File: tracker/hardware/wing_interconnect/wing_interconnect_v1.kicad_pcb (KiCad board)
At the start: 2 copper layers, 130 x 11 mm, 16 parts

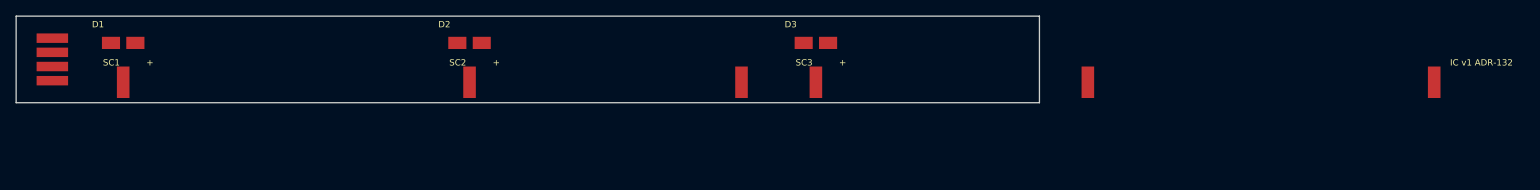
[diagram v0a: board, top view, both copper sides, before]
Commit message: feat(wing): 2-pin tab, GND+RF_FEED removed as dead copper, board is a small connector (ADR-134) (#286)
* feat(wing): foam wing geometry of record + ADR-130 (no PCB, parametric renders)

The wing stopped being a PCB when ADR-117 (Accepted by operator, 2026-10-15)
replaced the FR4 carrier with a bought XPS/Depron sheet. A foam wing has no
kicad_pcb, so `kicad-cli pcb render` has nothing to draw and the ONLY wing render
in the repo remained the RETIRED wing_board_v9 -- which is why the operator's
render still showed cells lying flat on copper.

Adds the missing geometry of record, parametric and cited:

* docs/analysis/foam_wing_geometry.py -- mass + VRML. Subtraction shown:
  cell 1.382 g (operator's own weighing) x 3 or 6; carrier = 0.1*rho*t*145.0 cm2;
  mount 0.15 g/cell (NIBBB measured, PANEL-MOUNTING-OFF-BOARD.md sec 2).
    EPS 3 mm SS 5.249 g | XPS 3 mm SS 5.988 g | XPS 6 mm SS 7.381 g
    EPS 3 mm DS 9.845 g | XPS 3 mm DS 10.584 g
    retired FR4 0.6 mm full-area 20.26 g (carrier 15.665 g)
* docs/analysis/render_foam_wing.py -- 6 PNG renders from the SAME parametric
  data (no VRML viewer on this host; matplotlib only), docs/fab/wing-3d/.
* docs/analysis/FOAM-WING-GEOMETRY-AND-MASS.md -- the two constructions (A foam
  plate, B foam spine), double-sided as option C, and the out-of-plane risk that
  picks the thickness; records that an earlier claim ("foam was never costed")
  was FALSE -- WING-MASS-FROM-MEASURED-CELLS.md sec 2 has the table and ADR-117
  accepted it.
* docs/analysis/WING-CUTOFF-AND-YAW.md -- cut survivability is ONE hub-side part
  (ADR-054 sec 2.2: without D_BP<n> the first cut kills the array, 0.00 W; with it
  only that wing's cells are lost). There is NO yaw authority (wing-jettison.md:
  "rotates slowly with no attitude control"), so shedding a wing neither helps nor
  hurts turn-around.
* docs/adr/130-foam-wing-geometry-authority.md -- number verified free via
  scripts/adr_next_number.py (--number 130 and --path both exit 0) and across 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
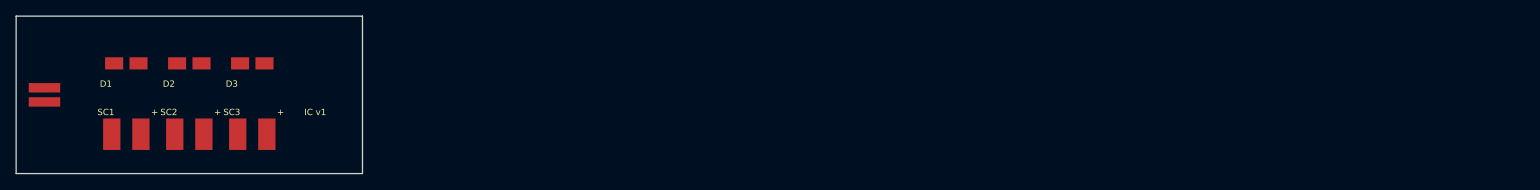
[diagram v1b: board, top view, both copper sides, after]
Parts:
- removed the ? at (4.60, 2.80)
- removed the ? at (180.2, 8.40)
- removed the ? at (12.1, 3.40)
- removed the ? at (15.2, 3.40)
- removed the ? at (56.0, 3.40)
- removed the ? at (59.1, 3.40)
- removed the ? at (100.0, 3.40)
- removed the ? at (103.2, 3.40)
- removed the ? at (4.60, 4.60)
- removed the ? at (4.60, 6.40)
- removed the ? at (4.60, 8.20)
- removed the ? at (13.6, 8.40)
- removed the ? at (92.2, 8.40)
- removed the ? at (57.6, 8.40)
- removed the ? at (136.2, 8.40)
- removed the ? at (101.6, 8.40)
- added ?: , wing_ic:J1, F.Cu at (3.60, 9.10)
- added ?: , wing_ic:D1, F.Cu at (15.6, 6.00)
- added ?: , wing_ic:D2, F.Cu at (20.4, 6.00)
- added ?: , wing_ic:D2, F.Cu at (23.6, 6.00)
- added ?: , wing_ic:D3, F.Cu at (28.4, 6.00)
- added ?: , wing_ic:D3, F.Cu at (31.6, 6.00)
- added ?: , wing_ic:J1, F.Cu at (3.60, 10.9)
- added ?: , wing_ic:SC1, F.Cu at (12.2, 15.0)
- added ?: , wing_ic:SC1, F.Cu at (15.8, 15.0)
- added ?: , wing_ic:SC2, F.Cu at (20.1, 15.0)
- added ?: , wing_ic:SC2, F.Cu at (23.9, 15.0)
- added ?: , wing_ic:SC3, F.Cu at (28.1, 15.0)
- added ?: , wing_ic:SC3, F.Cu at (31.9, 15.0)
- added ?: , wing_ic:D1, F.Cu at (12.4, 6.00)
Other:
- board size 130 x 11 mm -> 44 x 20 mm
- board text added: "IC v1"
- board text removed: "IC v1 ADR-132"
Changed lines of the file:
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@@
   (net 3 "SOLAR_MID2")
   (net 4 "SOLAR_N")
-  (net 5 "GND")
-  (net 6 "RF_FEED")
-  (gr_line (start 0 0) (end 130 0) (stroke (width 0.1) (type solid)) (layer "Edge.Cuts"))
-  (gr_line (start 130 0) (end 130 11) (stroke (width 0.1) (type solid)) (layer "Edge.Cuts"))
-  (gr_line (start 130 11) (end 0 11) (stroke (width 0.1) (type solid)) (layer "Edge.Cuts"))
-  (gr_line (start 0 11) (end 0 0) (stroke (width 0.1) (type solid)) (layer "Edge.Cuts"))
-  (footprint "wing_ic:J1" (layer "F.Cu") (at 4.6 2.8)
+  (gr_line (start 0 0) (end 44 0) (stroke (width 0.1) (type solid)) (layer "Edge.Cuts"))
+  (gr_line (start 44 0) (end 44 20) (stroke (width 0.1) (type solid)) (layer "Edge.Cuts"))
+  (gr_line (start 44 20) (end 0 20) (stroke (width 0.1) (type solid)) (layer "Edge.Cuts"))
+  (gr_line (start 0 20) (end 0 0) (stroke (width 0.1) (type solid)) (layer "Edge.Cuts"))
+  (footprint "wing_ic:J1" (layer "F.Cu") (at 3.6 9.1)
     (pad "1" smd rect (at 0 0) (size 4 1.2) (layers "F.Cu" "F.Paste" "F.Mask") (net 1 "SOLAR_P"))
   )
-  (footprint "wing_ic:J1" (layer "F.Cu") (at 4.6 4.6)
-    (pad "2" smd rect (at 0 0) (size 4 1.2) (layers "F.Cu" "F.Paste" "F.Mask") (net 2 "SOLAR_MID1"))
+  (footprint "wing_ic:J1" (layer "F.Cu") (at 3.6 10.9)
+    (pad "2" smd rect (at 0 0) (size 4 1.2) (layers "F.Cu" "F.Paste" "F.Mask") (net 4 "SOLAR_N"))
   )
-  (footprint "wing_ic:J1" (layer "F.Cu") (at 4.6 6.4)
-    (pad "3" smd rect (at 0 0) (size 4 1.2) (layers "F.Cu" "F.Paste" "F.Mask") (net 3 "SOLAR_MID2"))
+  (footprint "wing_ic:SC1" (layer "F.Cu") (at 12.15 15)
+    (pad "1" smd rect (at 0 0) (size 2.2 4) (layers "F.Cu" "F.Paste" "F.Mask") (net 1 "SOLAR_P"))
   )
-  (footprint "wing_ic:J1" (layer "F.Cu") (at 4.6 8.2)
-    (pad "4" smd rect (at 0 0) (size 4 1.2) (layers "F.Cu" "F.Paste" "F.Mask") (net 4 "SOLAR_N"))
+  (footprint "wing_ic:SC1" (layer "F.Cu") (at 15.85 15)
+    (pad "2" smd rect (at 0 0) (size 2.2 4) (layers "F.Cu" "F.Paste" "F.Mask") (net 2 "SOLAR_MID1"))
   )
-  (footprint "wing_ic:SC1" (layer "F.Cu") (at 13.6 8.4)
-    (pad "1" smd rect (at 0 0) (size 1.6 4) (layers "F.Cu" "F.Paste" "F.Mask") (net 1 "SOLAR_P"))
+  (footprint "wing_ic:SC2" (layer "F.Cu") (at 20.15 15)
+    (pad "1" smd rect (at 0 0) (size 2.2 4) (layers "F.Cu" "F.Paste" "F.Mask") (net 2 "SOLAR_MID1"))
   )
-  (footprint "wing_ic:SC1" (layer "F.Cu") (at 92.15 8.4)
-    (pad "2" smd rect (at 0 0) (size 1.6 4) (layers "F.Cu" "F.Paste" "F.Mask") (net 2 "SOLAR_MID1"))
+  (footprint "wing_ic:SC2" (layer "F.Cu") (at 23.85 15)
+    (pad "2" smd rect (at 0 0) (size 2.2 4) (layers "F.Cu" "F.Paste" "F.Mask") (net 3 "SOLAR_MID2"))
   )
-  (footprint "wing_ic:SC2" (layer "F.Cu") (at 57.6 8.4)
-    (pad "1" smd rect (at 0 0) (size 1.6 4) (layers "F.Cu" "F.Paste" "F.Mask") (net 2 "SOLAR_MID1"))
+  (footprint "wing_ic:SC3" (layer "F.Cu") (at 28.15 15)
+    (pad "1" smd rect (at 0 0) (size 2.2 4) (layers "F.Cu" "F.Paste" "F.Mask") (net 3 "SOLAR_MID2"))
   )
-  (footprint "wing_ic:SC2" (layer "F.Cu") (at 136.15 8.4)
-    (pad "2" smd rect (at 0 0) (size 1.6 4) (layers "F.Cu" "F.Paste" "F.Mask") (net 3 "SOLAR_MID2"))
+  (footprint "wing_ic:SC3" (layer "F.Cu") (at 31.85 15)
+    (pad "2" smd rect (at 0 0) (size 2.2 4) (layers "F.Cu" "F.Paste" "F.Mask") (net 4 "SOLAR_N"))
   )
-  (footprint "wing_ic:SC3" (layer "F.Cu") (at 101.6 8.4)
-    (pad "1" smd rect (at 0 0) (size 1.6 4) (layers "F.Cu" "F.Paste" "F.Mask") (net 3 "SOLAR_MID2"))
-  )
-  (footprint "wing_ic:SC3" (layer "F.Cu") (at 180.15 8.4)
-    (pad "2" smd rect (at 0 0) (size 1.6 4) (layers "F.Cu" "F.Paste" "F.Mask") (net 4 "SOLAR_N"))
-  )
-  (footprint "wing_ic:D1" (layer "F.Cu") (at 12.05 3.4)
+  (footprint "wing_ic:D1" (layer "F.Cu") (at 12.45 6)
     (pad "1" smd rect (at 0 0) (size 2.3 1.55) (layers "F.Cu" "F.Paste" "F.Mask") (net 1 "SOLAR_P"))
   )
-  (footprint "wing_ic:D1" (layer "F.Cu") (at 15.15 3.4)
+  (footprint "wing_ic:D1" (layer "F.Cu") (at 15.55 6)
     (pad "2" smd rect (at 0 0) (size 2.3 1.55) (layers "F.Cu" "F.Paste" "F.Mask") (net 2 "SOLAR_MID1"))
   )
-  (footprint "wing_ic:D2" (layer "F.Cu") (at 56.05 3.4)
+  (footprint "wing_ic:D2" (layer "F.Cu") (at 20.45 6)
     (pad "1" smd rect (at 0 0) (size 2.3 1.55) (layers "F.Cu" "F.Paste" "F.Mask") (net 2 "SOLAR_MID1"))
   )
-  (footprint "wing_ic:D2" (layer "F.Cu") (at 59.15 3.4)
+  (footprint "wing_ic:D2" (layer "F.Cu") (at 23.55 6)
     (pad "2" smd rect (at 0 0) (size 2.3 1.55) (layers "F.Cu" "F.Paste" "F.Mask") (net 3 "SOLAR_MID2"))
   )
-  (footprint "wing_ic:D3" (layer "F.Cu") (at 100.05 3.4)
+  (footprint "wing_ic:D3" (layer "F.Cu") (at 28.45 6)
     (pad "1" smd rect (at 0 0) (size 2.3 1.55) (layers "F.Cu" "F.Paste" "F.Mask") (net 3 "SOLAR_MID2"))
   )
-  (footprint "wing_ic:D3" (layer "F.Cu") (at 103.15 3.4)
+  (footprint "wing_ic:D3" (layer "F.Cu") (at 31.55 6)
     (pad "2" smd rect (at 0 0) (size 2.3 1.55) (layers "F.Cu" "F.Paste" "F.Mask") (net 4 "SOLAR_N"))
   )
-  (gr_text "SC1" (at 12.1 5.9) (layer "F.SilkS") (effects (font (size 0.8 0.8) (thickness 0.15))))
-  (gr_text "+" (at 17 5.9) (layer "F.SilkS") (effects (font (size 0.8 0.8) (thickness 0.15))))
-  (gr_text "SC2" (at 56.1 5.9) (layer "F.SilkS") (effects (font (size 0.8 0.8) (thickness 0.15))))
-  (gr_text "+" (at 61 5.9) (layer "F.SilkS") (effects (font (size 0.8 0.8) (thickness 0.15))))
-  (gr_text "SC3" (at 100.1 5.9) (layer "F.SilkS") (effects (font (size 0.8 0.8) (thickness 0.15))))
-  (gr_text "+" (at 105 5.9) (layer "F.SilkS") (effects (font (size 0.8 0.8) (thickness 0.15))))
-  (gr_text "D1" (at 10.4 1.05) (layer "F.SilkS") (effects (font (size 0.8 0.8) (thickness 0.15))))
-  (gr_text "D2" (at 54.4 1.05) (layer "F.SilkS") (effects (font (size 0.8 0.8) (thickness 0.15))))
-  (gr_text "D3" (at 98.4 1.05) (layer "F.SilkS") (effects (font (size 0.8 0.8) (thickness 0.15))))
-  (gr_text "IC v1 ADR-132" (at 186.15 5.9) (layer "F.SilkS") (effects (font (size 0.8 0.8) (thickness 0.15))))
+  (gr_text "SC1" (at 11.4 12.2) (layer "F.SilkS") (effects (font (size 0.8 0.8) (thickness 0.15))))
+  (gr_text "+" (at 17.6 12.2) (layer "F.SilkS") (effects (font (size 0.8 0.8) (thickness 0.15))))
+  (gr_text "SC2" (at 19.4 12.2) (layer "F.SilkS") (effects (font (size 0.8 0.8) (thickness 0.15))))
+  (gr_text "+" (at 25.6 12.2) (layer "F.SilkS") (effects (font (size 0.8 0.8) (thickness 0.15))))
+  (gr_text "SC3" (at 27.4 12.2) (layer "F.SilkS") (effects (font (size 0.8 0.8) (thickness 0.15))))
+  (gr_text "+" (at 33.6 12.2) (layer "F.SilkS") (effects (font (size 0.8 0.8) (thickness 0.15))))
+  (gr_text "D1" (at 11.4 8.6) (layer "F.SilkS") (effects (font (size 0.8 0.8) (thickness 0.15))))
+  (gr_text "D2" (at 19.4 8.6) (layer "F.SilkS") (effects (font (size 0.8 0.8) (thickness 0.15))))
+  (gr_text "D3" (at 27.4 8.6) (layer "F.SilkS") (effects (font (size 0.8 0.8) (thickness 0.15))))
+  (gr_text "IC v1" (at 38 12.2) (layer "F.SilkS") (effects (font (size 0.8 0.8) (thickness 0.15))))
 )

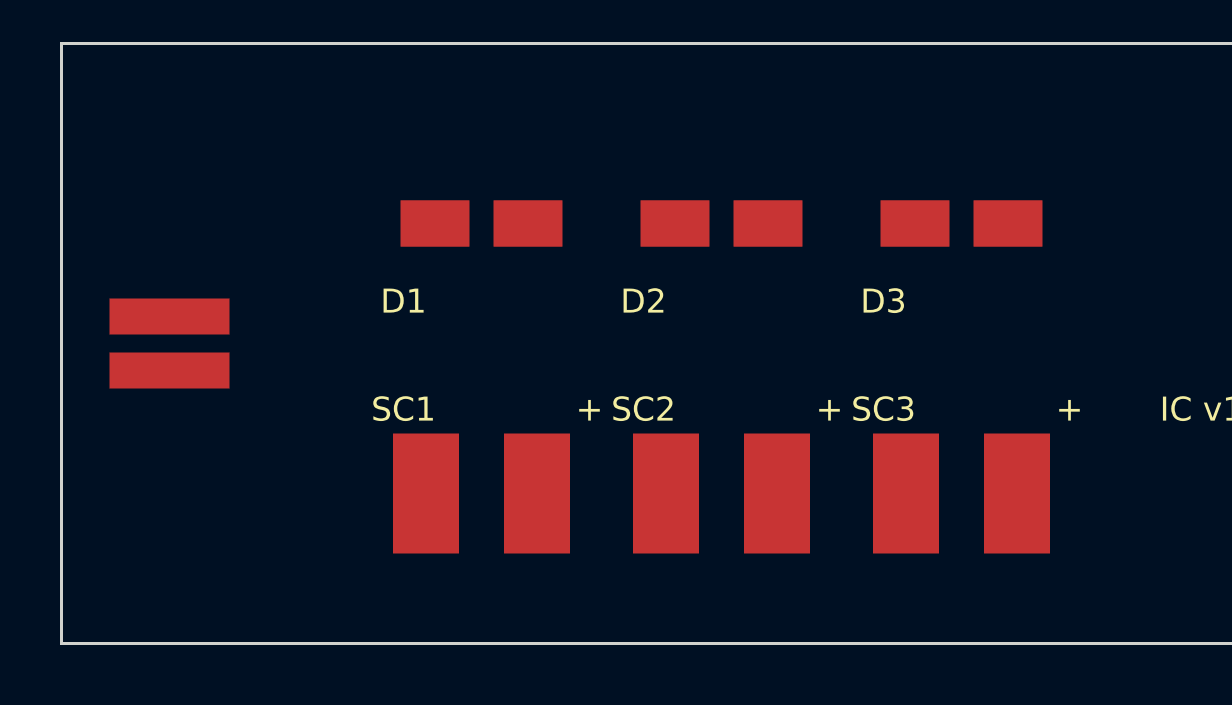
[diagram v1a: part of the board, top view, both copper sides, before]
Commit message: feat(wing): interconnect board ROUTED -- 0 unrouted, 0 electrical DRC violations
The wing interconnect board is now fully routed. DRC on the committed board:
  7 lib_footprint_issues   (generated footprints, no registered library -- same as hub)
  0 everything else        (no short, clearance, crossing, mask bridge, silk or edge)
KiCad's own connectivity engine, independent of DRC: unrouted = 0.
7 footprints, 14 pads, 34 tracks.

ROUTING IS TWO MECHANISMS, DELIBERATELY
  * deterministic geometry in the generator for the two COLLINEAR nets. SOLAR_P and
    SOLAR_N have pads at identical x, one row at y=6 and one at y=15, so they are straight
    vertical drops. P stays on F.Cu (its column at x=12.15 is left of every MID pad).
    N's horizontal escape runs on B.Cu -- on F.Cu it CANNOT work, because the pad rows sit
    at y=6 and y=15 and P's column spans exactly that range, so no clear y exists on one
    layer. Two vias lift it over.
  * the A* router for the two multi-pad nets:
    route_v10_astar.py --append --nets SOLAR_MID1,SOLAR_MID2  -> routed 2, failed 0.
  Router alone measured 2 of 4 nets maximum in every ordering tried (--promote included);
  making two nets trivial by construction is what closed the rest.

SIX DEFECTS FOUND AND FIXED, ALL MEASURED (docs/fab/wing-3d/ROUTING-STATUS.md sec 3)
  1 one footprint PER PAD -> 14 footprints for 7 parts (group pads by ref)
  2 removing fp_text reference to fix silk_overlap DESTROYED NET IDENTITY -- every ref read
    identical, so the router deduped SOLAR_P's 3 pads to 1 and silently skipped the net
    ("failed 0", 2 of 4 routed). Restored on F.Fab so silk stays clean and identity holds.
    LESSON: a silk fix must never touch the reference property.
  3 router clobber guard hardcoded "nfps < 20" / "expected 28" (the hub's count), so a
    7-part board could never be saved; now --expect-footprints, default 20, hub unchanged
  4 cells cx+-1.85 vs diodes cx+-1.55 staggered every net into a TRIANGLE; one PAD_DX make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
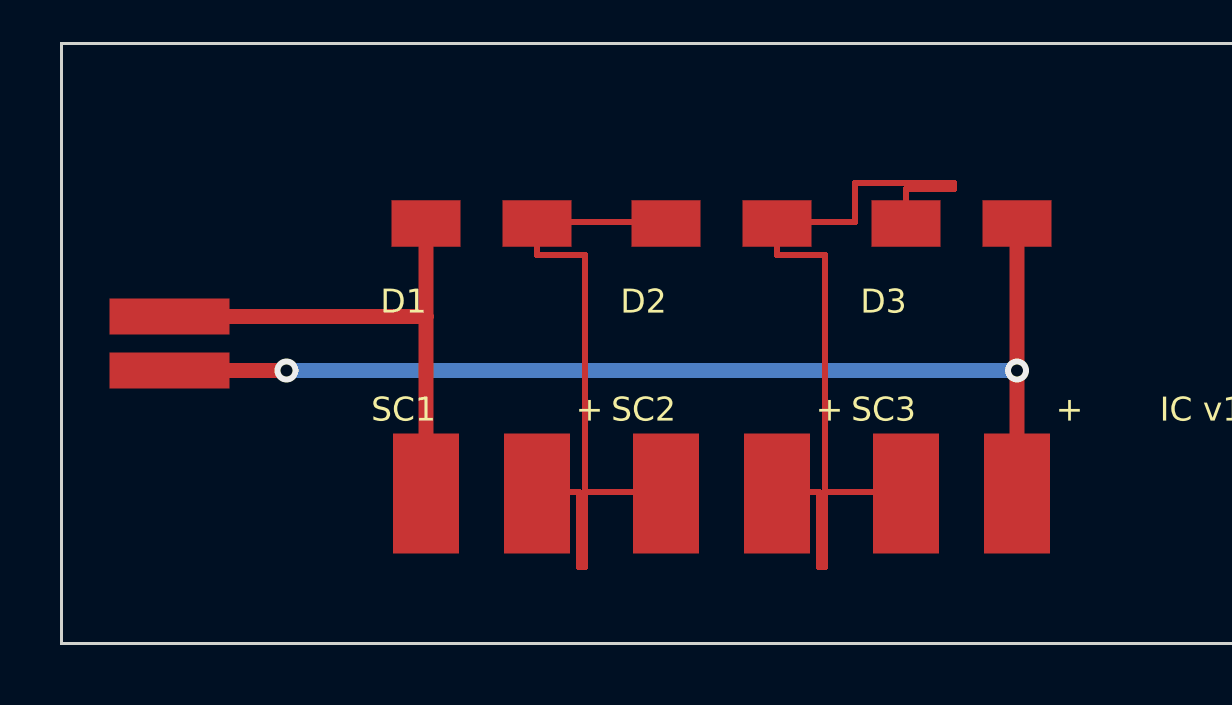
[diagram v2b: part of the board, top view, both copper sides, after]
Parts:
- removed ? (x2): , wing_ic:J1
- removed ? (x2): , wing_ic:D1
- removed ? (x2): , wing_ic:D2
- removed ? (x2): , wing_ic:D3
- removed ? (x2): , wing_ic:SC1
- removed ? (x2): , wing_ic:SC2
- removed ? (x2): , wing_ic:SC3
- added D1: , wing_ic:D1, F.Cu at (12.2, 6.00)
- added D2: , wing_ic:D2, F.Cu at (20.1, 6.00)
- added D3: , wing_ic:D3, F.Cu at (28.1, 6.00)
- added J1: , wing_ic:J1, F.Cu at (3.60, 9.10)
- added SC1: , wing_ic:SC1, F.Cu at (12.2, 15.0)
- added SC2: , wing_ic:SC2, F.Cu at (20.1, 15.0)
- added SC3: , wing_ic:SC3, F.Cu at (28.1, 15.0)
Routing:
- net SOLAR_N: track 0.00 -> 37.2 mm, vias 0 -> 2
- net SOLAR_MID2: track 0.00 -> 32.7 mm
- net SOLAR_MID1: track 0.00 -> 26.9 mm
- net SOLAR_P: track 0.00 -> 17.6 mm

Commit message: feat(wing): real wing_ic footprint library -- board is now DRC-clean, 0 violations (#292)
THE LAST FAB BLOCKER IS GONE. kicad-cli pcb drc --exit-code-violations now reports:

    Found 0 violations
    Found 0 unconnected items

Previously it reported 7 x lib_footprint_issues. Zero violations of ANY class -- no lib
warnings, no shorts, no clearance, no crossings, no mask bridges, no silk, no edge.

ROOT CAUSE WAS NAMING, NOT GEOMETRY
DRC said, seven times: "The current configuration does not include the footprint library
'wing_ic'." The board's pads were in the right places; they named a library that did not
exist, so nothing could resolve and the board could never be ordered.

THE FIX, following the pattern the repo already uses (balloon_flight.pretty + ${KIPRJMOD}):
  * tracker/hardware/wing_interconnect/wing_ic.pretty/ -- D_SMA_Wing, SolarTail_2P, Tab_2P
  * tracker/hardware/wing_interconnect/fp-lib-table -- registers it
  * tracker/hardware/build_wing_footprints.py -- deterministic generator (--check)

LAND GEOMETRY IS CARRIED OVER UNCHANGED, DELIBERATELY
The pads reproduce the board's existing patterns, NOT the stock vendor ones:
    stock Diode_SMD:D_SMA   2.5 x 1.8 at +-2.0
    this board              2.3 x 1.55 at +-1.85
Adopting the stock pattern would move every pad edge by up to 0.2 mm and invalidate the
routed copper from PR #289 -- to fix a NAMING problem. The house pattern is frozen as a
named library footprint and the deviation from the vendor land pattern is recorded rather
than silently adopted.

THE BOARD EMITS THE LIBRARY FOOTPRINT VERBATIM
Writing the body by hand produced 7 x lib_footprint_mismatch (measured): DRC compares the
board's embedded copy against the library file and any difference -- courtyard, pad order --
is a warning. build_wing_interconnect.py now reads the .kicad_mod and substitutes only the
origin, the reference and the per-pad nets, so a mismatch is impossible by construction.

FOUR DEFECTS FOUND WHILE DOING IT, ALL MEASURED
  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
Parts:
- D1: value (none) -> D_SMA_Wing; footprint wing_ic:D1 -> wing_ic:D_SMA_Wing
- D2: value (none) -> D_SMA_Wing; footprint wing_ic:D2 -> wing_ic:D_SMA_Wing
- D3: value (none) -> D_SMA_Wing; footprint wing_ic:D3 -> wing_ic:D_SMA_Wing
- J1: value (none) -> Tab_2P; footprint wing_ic:J1 -> wing_ic:Tab_2P
- SC1: value (none) -> SolarTail_2P; footprint wing_ic:SC1 -> wing_ic:SolarTail_2P
- SC2: value (none) -> SolarTail_2P; footprint wing_ic:SC2 -> wing_ic:SolarTail_2P
- SC3: value (none) -> SolarTail_2P; footprint wing_ic:SC3 -> wing_ic:SolarTail_2P
- moved D2 1.85 mm to (22.0, 6.00)
- moved D3 1.85 mm to (30.0, 6.00)
- moved SC2 1.85 mm to (22.0, 15.0)
- moved SC3 1.85 mm to (30.0, 15.0)
- moved D1 1.85 mm to (14.0, 6.00)
- moved SC1 1.85 mm to (14.0, 15.0)
- moved J1 0.90 mm to (3.60, 10.0)
